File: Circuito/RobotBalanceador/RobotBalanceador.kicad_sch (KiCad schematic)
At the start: 62 parts, among them J1 ICSP, J2 USB_B_Micro, J3 Barrel_Jack_Switch, J4 ENCODER, J5 ENCODER, J6 MOT 1, J7 MOT 2, U1 STM32F103C8Tx, U2 LMR62014XMF, U3 AMS1117-3.3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

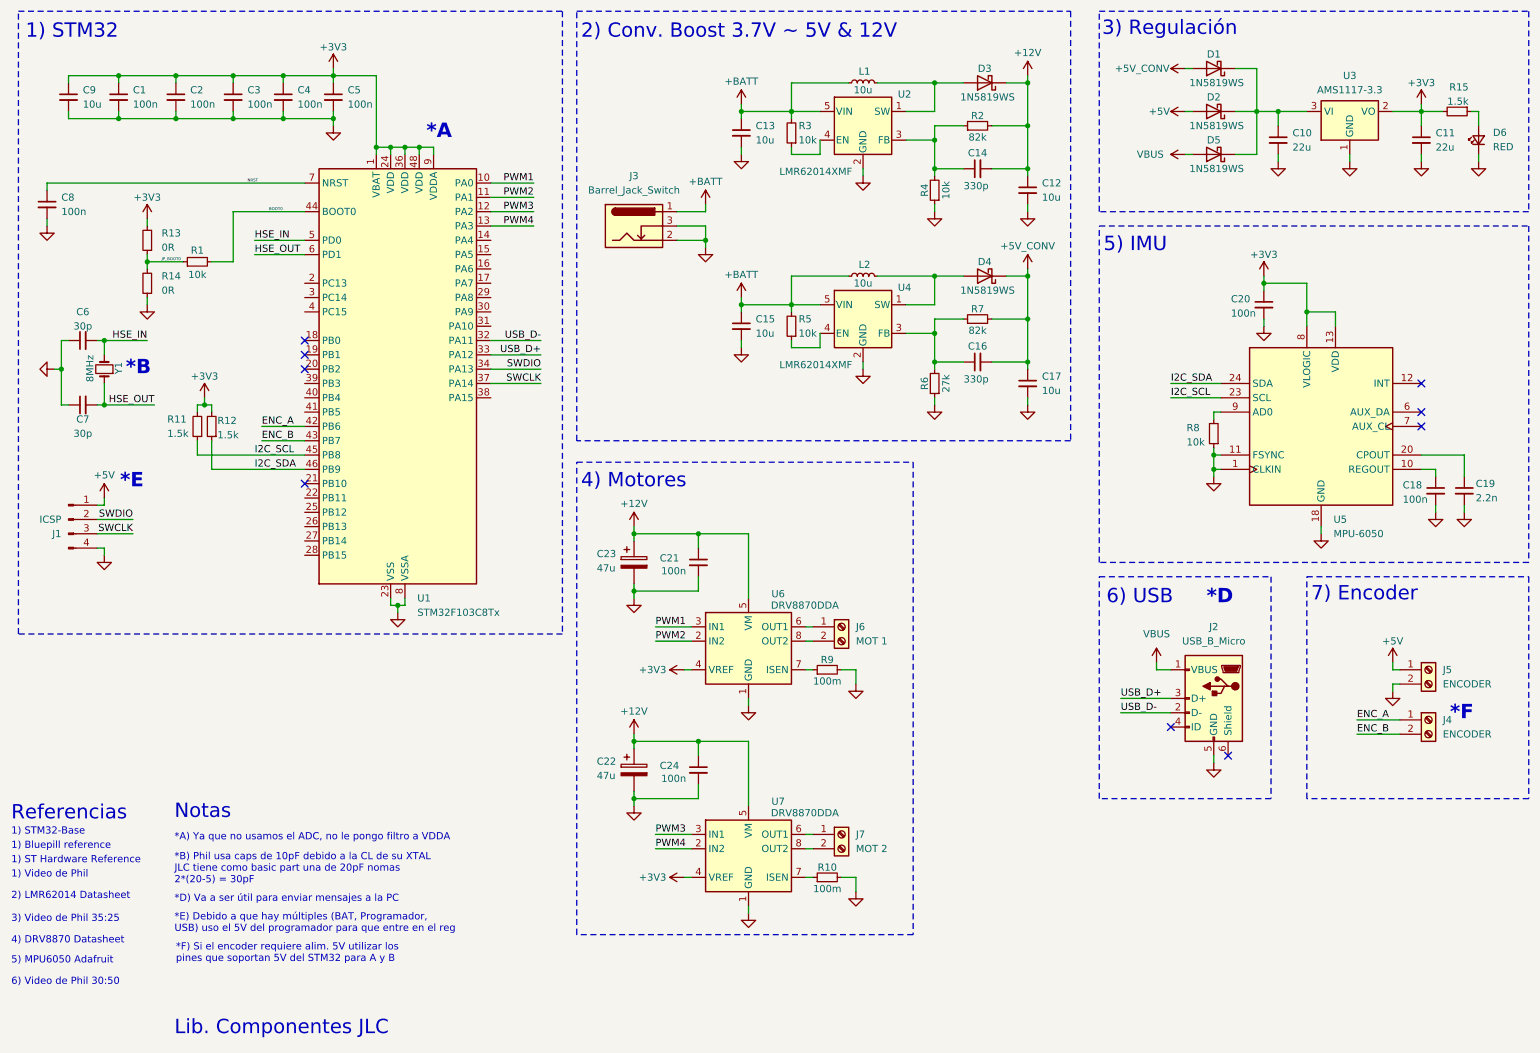
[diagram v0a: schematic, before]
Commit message: Reasig. de pines, TIM3 p/ PWM, I2C2 p/ IMU y Comps. colocados en PCB
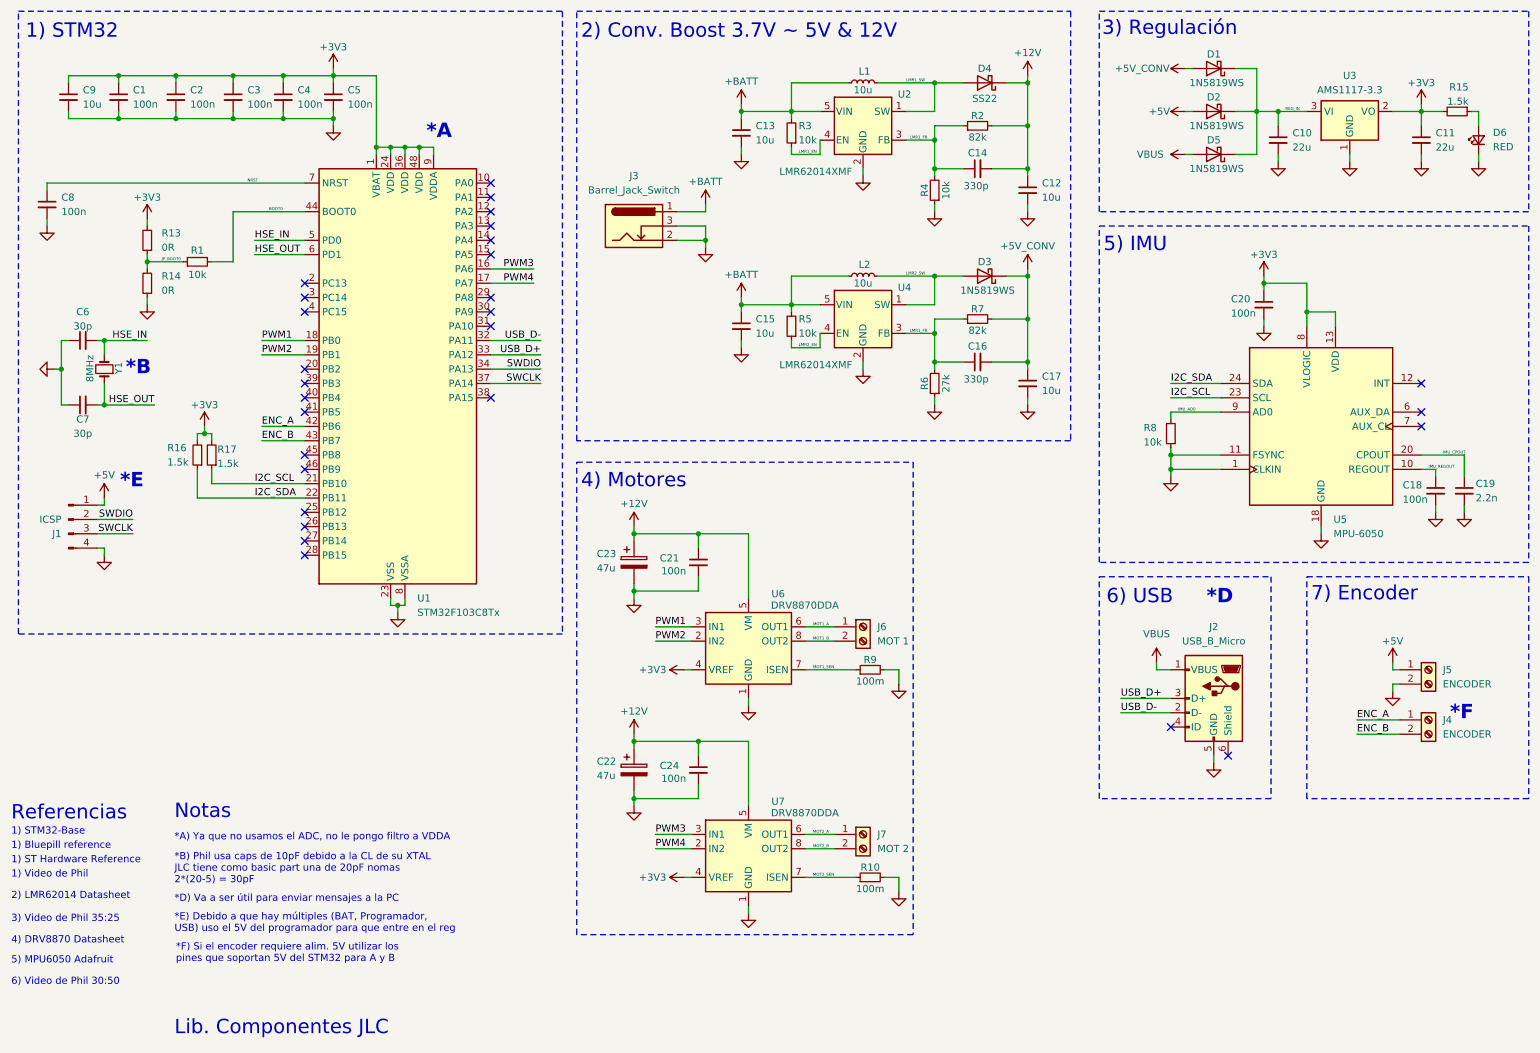
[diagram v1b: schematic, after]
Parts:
- removed D4: 1N5819WS, Diode_SMD:D_SOD-323, symbol Diode:1N5819WS
- removed R11, R12: 1.5k, Resistor_SMD:R_0603_1608Metric, symbol Device:R_Small
- added D4: SS22, Diode_SMD:D_SMA, symbol Diode:SS22
- added R16, R17: 1.5k, Resistor_SMD:R_0603_1608Metric, symbol Device:R_Small
- Y1: footprint Crystal:Crystal_SMD_HC49-SD -> Crystal:Crystal_SMD_5032-2Pin_5.0x3.2mm; JLCPCB C12674 -> C115962; Link https://jlcpcb.com/partdetail/Yxc_CrystalOscillators-X49SM8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 -> https://jlcpcb.com/partdetail/Yxc_CrystalOscillators-X50328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
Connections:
- net +12V: now also D4.1 (K); no longer D3.1 (K)
- net +3V3: now also R16.2, R17.2
- net +5V_CONV: now also D3.1 (K)
- net I2C_SCL: now also U1.21 (PB10), R17.1; no longer U1.45 (PB8)
- net I2C_SDA: now also U1.22 (PB11), R16.1; no longer U1.46 (PB9)
- net PWM1: now also U1.18 (PB0); no longer U1.10 (PA0)
- net PWM2: now also U1.19 (PB1); no longer U1.11 (PA1)
- net PWM3: now also U1.16 (PA6); no longer U1.12 (PA2)
- net PWM4: now also U1.17 (PA7); no longer U1.13 (PA3)
- net REG_IN: now reaches C10.1, D1.1 (K), D2.1 (K), D5.1 (K), U3.3 (VI)
- net MOT2_SEN: now reaches R10.1, U7.7 (ISEN)
- net LMR2_SW: now reaches L2.2, U4.1 (SW)
- net LMR2_SW: now also D3.2 (A)
- net LMR1_FB: now reaches C16.1, R6.2, R7.1, U4.3 (FB)
- net LMR1_FB: now also C14.1, R2.1, R4.2, U2.3 (FB)
- net LMR2_EN: now reaches R5.1, U4.4 (EN)
- net MOT1_SEN: now reaches R9.1, U6.7 (ISEN)
- net LMR1_SW: now reaches L1.2, U2.1 (SW)
- net LMR1_SW: now also D4.2 (A); no longer D3.2 (A)
- net MOT1_A: now reaches J6.1 (Pin_1), U6.6 (OUT1)
- net MOT1_B: now reaches J6.2 (Pin_2), U6.8 (OUT2)
- net IMU_AD0: now reaches R8.2, U5.9 (AD0)
- net IMU_REGOUT: now reaches C18.1, U5.10 (REGOUT)
- net IMU_CPOUT: now reaches C19.1, U5.20 (CPOUT)
- net LMR1_EN: now reaches R3.1, U2.4 (EN)
- net MOT2_A: now reaches J7.1 (Pin_1), U7.6 (OUT1)
- net MOT2_B: now reaches J7.2 (Pin_2), U7.8 (OUT2)
- no-connect marks 9 -> 28
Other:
- moved on the sheet: J6, J7, R10, R8, R9

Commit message: Ruteado inicial de tracks
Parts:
- removed R13, R14: 0R, Resistor_SMD:R_0402_1005Metric, symbol Device:R_Small
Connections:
- net JP_BOOT0 is gone; now on net GND: R1.1
- net +5V: no longer J5.1 (Pin_1)
- net +5V_CONV: now also J5.1 (Pin_1)
- net LMR1_FB: no longer C16.1, R6.2, R7.1, U4.3 (FB)
- net LED_ANODE: now reaches D6.2 (A), R15.1
- new net LMR2_FB: C16.1, R6.2, R7.1, U4.3 (FB)
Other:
- moved on the sheet: R1

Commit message: Ruteado completo, gerbers generados
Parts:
- removed D4: SS22, Diode_SMD:D_SMA, symbol Diode:SS22
- added D4: 1N5819WS, Diode_SMD:D_SOD-323, symbol Diode:1N5819WS
- added R11: 1.5k, Resistor_SMD:R_0603_1608Metric, symbol Device:R_Small
- C1, C18, C2, C20, C21, C24, C3, C4, C5, C8: JLCPCB C14663 -> (none); LCSC (none) -> C14663
- C10, C11: JLCPCB C45783 -> (none); LCSC (none) -> C45783
- C12, C13, C15, C17, C9: JLCPCB C19702 -> (none); LCSC (none) -> C19702
- C14, C16: JLCPCB C1664 -> (none); LCSC (none) -> C1664
- C19: JLCPCB C1604 -> (none); LCSC (none) -> C1604
- C22, C23: JLCPCB C2836440 -> (none); LCSC (none) -> C2836440
- C6: JLCPCB C1658 -> (none); LCSC (none) -> C1658
- C7: JLCPCB C1648 -> (none); LCSC (none) -> C1648
- D1, D2, D3, D5: JLCPCB C191023 -> (none); LCSC (none) -> C191023
- D6: JLCPCB C2286 -> (none); LCSC (none) -> C2286
- J1: LCSC (none) -> C6332197; Link (none) -> https://www.lcsc.com/product-detail/Pin-Headers_Hanbo-Elect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
- J2: footprint Connector_USB:USB_Micro-AB_Molex_47590-0001 -> Connector_USB:USB_Micro-B_Molex-105017-0001; JLCPCB C136001 -> (none); LCSC (none) -> C136000; Link https://jlcpcb.com/partdetail/Molex-475900001/C136001 -> https://jlcpcb.com/partdetail/Molex-1050170001/C136000
- J3: LCSC (none) -> C5280493; Link (none) -> https://www.lcsc.com/product-detail/New-Arrivals_Global-Con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
- J4, J5, J6, J7: JLCPCB C474906 -> (none); LCSC (none) -> C474906
- L1, L2: JLCPCB C602018 -> (none); LCSC (none) -> C602018
- R1, R3, R4, R5, R8: JLCPCB C25804 -> (none); LCSC (none) -> C25804
- R10, R9: JLCPCB C25334 -> (none); LCSC (none) -> C25334
- R15, R16, R17: JLCPCB C22843 -> (none); LCSC (none) -> C22843
- R2, R7: JLCPCB C23254 -> (none); LCSC (none) -> C23254
- R6: JLCPCB C22967 -> (none); LCSC (none) -> C22967
- U1: JLCPCB C8734 -> (none); LCSC (none) -> C8734
- U2, U4: JLCPCB C55182 -> (none); LCSC (none) -> C55182
- U3: JLCPCB C6186 -> (none); LCSC (none) -> C6186
- U5: LCSC (none) -> C24112; Link (none) -> https://jlcpcb.com/partdetail/TdkInvensense-MPU6050/C24112
- U6, U7: JLCPCB C86590 -> (none); LCSC (none) -> C86590
- Y1: JLCPCB C115962 -> (none); LCSC (none) -> C115962
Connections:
- net +12V: now also D4.1 (K)
- net +3V3: now also R11.2
- net LMR1_SW: now also D4.2 (A)
- net USB_D+: now also R11.1
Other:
- moved on the sheet: C8, J2

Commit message: Modificaciones a USB y ruteado
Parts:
- J2: footprint Connector_USB:USB_Micro-B_Molex-105017-0001 -> Connector_USB:USB_Micro-B_Molex_47346-0001; LCSC C136000 -> C132560; Link https://jlcpcb.com/partdetail/Molex-1050170001/C136000 -> https://jlcpcb.com/partdetail/Molex-473460001/C132560
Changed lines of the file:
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@@
 			)
 		)
-		(property "Footprint" "Connector_USB:USB_Micro-B_Molex-105017-0001"
+		(property "Footprint" "Connector_USB:USB_Micro-B_Molex_47346-0001"
 			(at 228.6 137.16 0)
 			(effects
@@
 			)
 		)
-		(property "Datasheet" "https://wmsc.lcsc.com/wmsc/upload/file/pdf/v2/lcsc/2407041202_MOLEX-1050170001_C136000.pdf"
+		(property "Datasheet" "https://www.molex.com/en-us/products/part-detail/473460001?display=pdf"
 			(at 228.6 137.16 0)
 			(effects
@@
 			)
 		)
-		(property "LCSC" "C136000"
+		(property "LCSC" "C132560"
 			(at 232.41 135.89 0)
 			(effects
@@
 			)
 		)
-		(property "Link" "https://jlcpcb.com/partdetail/Molex-1050170001/C136000"
+		(property "Link" "https://jlcpcb.com/partdetail/Molex-473460001/C132560"
 			(at 232.41 135.89 0)
 			(effects
